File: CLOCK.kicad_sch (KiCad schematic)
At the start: 6 parts, among them X1 S3D50.000000B20F30T

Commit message: DO the bulk of rev 1.2 layout
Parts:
- removed JP3: CLK_EN pull, Jumper:SolderJumper-3_P1.3mm_Bridged12_RoundedPad1.0x1.5mm, symbol Jumper:SolderJumper_3_Bridged12
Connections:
- net CLK_EN: now also R24.1; no longer R24.2
- net GND: now also R24.2
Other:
- moved on the sheet: R24
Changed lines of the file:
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@@
 	(paper "A4")
+	(junction
+		(at 127 96.52)
+		(diameter 0)
+		(color 0 0 0 0)
+	)
 	(junction
 		(at 134.62 96.52)
@@
 	(wire
 		(pts
-			(xy 134.62 80.01) (xy 134.62 85.09)
-		)
-		(stroke
-			(width 0)
-			(type default)
-		)
-	)
-	(wire
-		(pts
 			(xy 153.035 83.82) (xy 153.035 88.9)
 		)
@@
 	(wire
 		(pts
-			(xy 127 76.2) (xy 127 80.01)
-		)
-		(stroke
-			(width 0)
-			(type default)
-		)
-	)
-	(wire
-		(pts
 			(xy 188.595 100.33) (xy 188.595 103.505)
 		)
@@
 	(wire
 		(pts
-			(xy 142.24 76.2) (xy 142.24 72.39)
-		)
-		(stroke
-			(width 0)
-			(type default)
-		)
-	)
-	(wire
-		(pts
-			(xy 134.62 96.52) (xy 134.62 92.71)
-		)
-		(stroke
-			(width 0)
-			(type default)
-		)
-	)
-	(wire
-		(pts
-			(xy 127.635 96.52) (xy 134.62 96.52)
+			(xy 127 107.95) (xy 127 111.76)
+		)
+		(stroke
+			(width 0)
+			(type default)
+		)
+	)
+	(wire
+		(pts
+			(xy 127 96.52) (xy 134.62 96.52)
+		)
+		(stroke
+			(width 0)
+			(type default)
+		)
+	)
+	(wire
+		(pts
+			(xy 118.11 96.52) (xy 127 96.52)
 		)
 		(stroke
@@
 	(wire
 		(pts
-			(xy 139.7 76.2) (xy 142.24 76.2)
-		)
-		(stroke
-			(width 0)
-			(type default)
-		)
-	)
-	(wire
-		(pts
-			(xy 127 76.2) (xy 129.54 76.2)
+			(xy 127 96.52) (xy 127 100.33)
 		)
 		(stroke
@@
 	(hierarchical_label "CLK_EN"
 		(shape input)
-		(at 127.635 96.52 180)
+		(at 118.11 96.52 180)
 		(effects
 			(font
@@
 	(symbol
 		(lib_id "power:GND")
-		(at 127 80.01 0)
+		(at 127 111.76 0)
 		(unit 1)
 		(exclude_from_sim no)
@@
 		(fields_autoplaced yes)
 		(property "Reference" "#PWR08"
-			(at 127 86.36 0)
+			(at 127 118.11 0)
 			(effects
 				(font
@@
 		)
 		(property "Value" "GND"
-			(at 127 85.09 0)
+			(at 127 116.84 0)
 			(effects
 				(font
@@
 		)
 		(property "Footprint" ""
-			(at 127 80.01 0)
+			(at 127 111.76 0)
 			(effects
 				(font
@@
 		)
 		(property "Datasheet" ""
-			(at 127 80.01 0)
+			(at 127 111.76 0)
 			(effects
 				(font
@@
 		)
 		(property "Description" ""
-			(at 127 80.01 0)
+			(at 127 111.76 0)
 			(effects
 				(font
@@
 	(symbol
 		(lib_id "Device:R")
-		(at 134.62 88.9 0)
+		(at 127 104.14 0)
 		(unit 1)
 		(exclude_from_sim no)
@@
 		(on_board yes)
 		(dnp no)
-		(fields_autoplaced yes)
 		(property "Reference" "R24"
-			(at 137.16 87.6299 0)
+			(at 120.396 102.616 0)
 			(effects
 				(font
@@
 		)
 		(property "Value" "10k"
-			(at 137.16 90.1699 0)
+			(at 120.396 105.156 0)
 			(effects
 				(font
@@
 		)
 		(property "Footprint" "Resistor_SMD:R_0603_1608Metric_Pad0.98x0.95mm_HandSolder"
-			(at 132.842 88.9 90)
+			(at 125.222 104.14 90)
 			(effects
 				(font
@@
 		)
 		(property "Datasheet" "~"
-			(at 134.62 88.9 0)
+			(at 127 104.14 0)
 			(effects
 				(font
@@
 		)
 		(property "Description" ""
-			(at 134.62 88.9 0)
+			(at 127 104.14 0)
 			(effects
 				(font
@@
 		)
 		(property "LCSC" "C2930027"
-			(at 134.62 88.9 0)
+			(at 127 104.14 0)
 			(effects
 				(font
@@
 					(unit 1)
 				)
-			)
-		)
-	)
-	(symbol
-		(lib_id "power:+3.3V")
-		(at 142.24 72.39 0)
-		(unit 1)
-		(exclude_from_sim no)
-		(in_bom yes)
-		(on_board yes)
-		(dnp no)
-		(fields_autoplaced yes)
-		(property "Reference" "#PWR049"
-			(at 142.24 76.2 0)
-			(effects
-				(font
-					(size 1.27 1.27)
-				)
-				(hide yes)
-			)
-		)
-		(property "Value" "+3.3V"
-			(at 142.24 67.31 0)
-			(effects
-				(font
-					(size 1.27 1.27)
-				)
-			)
-		)
-		(property "Footprint" ""
-			(at 142.24 72.39 0)
-			(effects
-				(font
-					(size 1.27 1.27)
-				)
-				(hide yes)
-			)
-		)
-		(property "Datasheet" ""
-			(at 142.24 72.39 0)
-			(effects
-				(font
-					(size 1.27 1.27)
-				)
-				(hide yes)
-			)
-		)
-		(property "Description" ""
-			(at 142.24 72.39 0)
-			(effects
-				(font
-					(size 1.27 1.27)
-				)
-				(hide yes)
-			)
-		)
-		(pin "1"
-		)
-		(instances
-			(project ""
-				(path "/727d6c0a-a0ef-4feb-9656-3db3cb90564a/2418ed7a-6668-472e-9550-09c70e5c9c72"
-					(reference "#PWR049")
-					(unit 1)
-				)
-			)
-		)
-	)
-	(symbol
-		(lib_id "Jumper:SolderJumper_3_Bridged12")
-		(at 134.62 76.2 0)
-		(unit 1)
-		(exclude_from_sim yes)
-		(in_bom no)
-		(on_board yes)
-		(dnp no)
-		(fields_autoplaced yes)
-		(property "Reference" "JP3"
-			(at 134.62 69.85 0)
-			(effects
-				(font
-					(size 1.27 1.27)
-				)
-			)
-		)
-		(property "Value" "CLK_EN pull"
-			(at 134.62 72.39 0)
-			(effects
-				(font
-					(size 1.27 1.27)
-				)
-			)
-		)
-		(property "Footprint" "Jumper:SolderJumper-3_P1.3mm_Bridged12_RoundedPad1.0x1.5mm"
-			(at 134.62 76.2 0)
-			(effects
-				(font
-					(size 1.27 1.27)
-				)
-				(hide yes)
-			)
-		)
-		(property "Datasheet" "~"
-			(at 134.62 76.2 0)
-			(effects
-				(font
-					(size 1.27 1.27)
-				)
-				(hide yes)
-			)
-		)
-		(property "Description" "3-pole Solder Jumper, pins 1+2 closed/bridged"
-			(at 134.62 76.2 0)
-			(effects
-				(font
-					(size 1.27 1.27)
-				)
-				(hide yes)
-			)
-		)
-		(pin "1"
-		)
-		(pin "2"
-		)
-		(pin "3"
-		)
-		(instances
-			(project ""
-				(path "/727d6c0a-a0ef-4feb-9656-3db3cb90564a/2418ed7a-6668-472e-9550-09c70e5c9c72"
-					(reference "JP3")
-					(unit 1)
-				)

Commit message: Use kicad symbol for the optotransistor
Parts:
- X1: footprint project specific:XTAL_TSX-3225_16.0000MF18X-AC3 -> project_footprints:XTAL_TSX-3225_16.0000MF18X-AC3
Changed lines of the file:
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@@
 			)
 		)
-		(property "Footprint" "project specific:XTAL_TSX-3225_16.0000MF18X-AC3"
+		(property "Footprint" "project_footprints:XTAL_TSX-3225_16.0000MF18X-AC3"
 			(at 170.815 105.41 0)
 			(effects

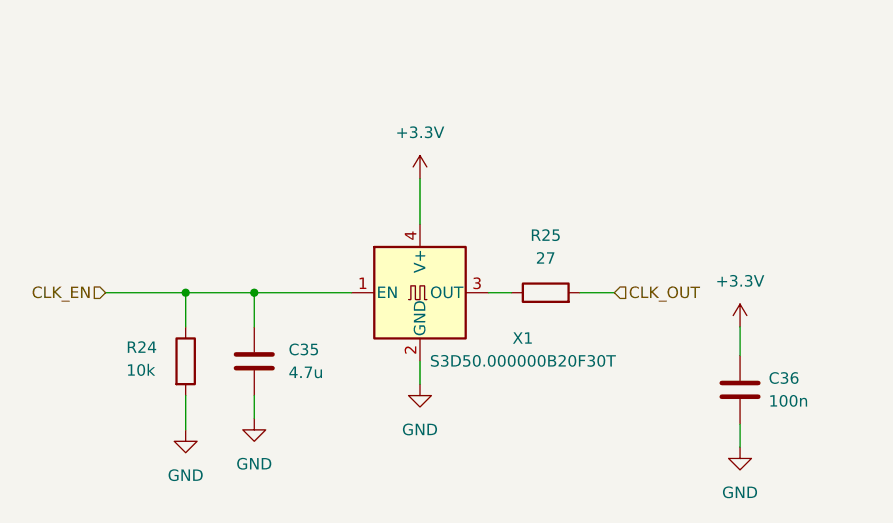
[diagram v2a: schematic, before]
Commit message: Update crystal LCSC number, use built-in footprint
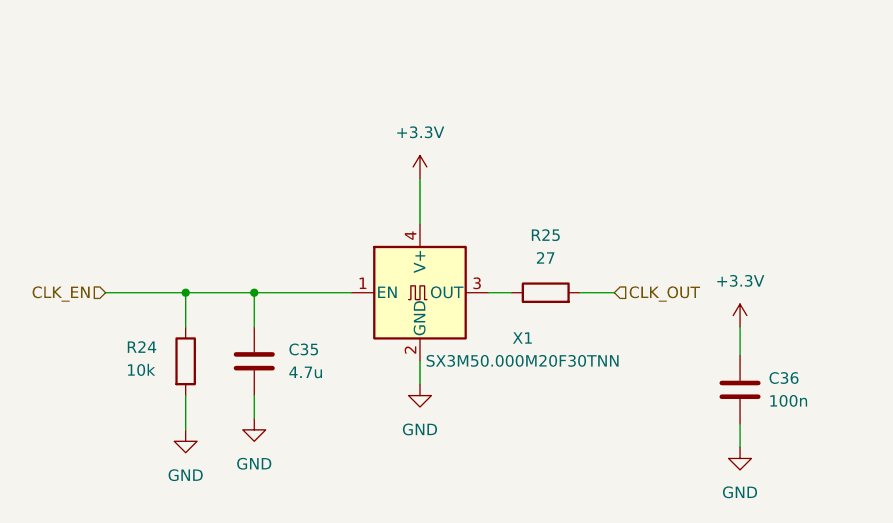
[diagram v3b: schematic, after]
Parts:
- X1: value S3D50.000000B20F30T -> SX3M50.000M20F30TNN; footprint project_footprints:XTAL_TSX-3225_16.0000MF18X-AC3 -> Oscillator:Oscillator_SMD_EuroQuartz_XO32-4Pin_3.2x2.5mm; LCSC C387445 -> C2901592
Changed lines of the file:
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@@
 			)
 		)
-		(property "Value" "S3D50.000000B20F30T"
+		(property "Value" "SX3M50.000M20F30TNN"
 			(at 164.465 104.14 0)
 			(effects
@@
 			)
 		)
-		(property "Footprint" "project_footprints:XTAL_TSX-3225_16.0000MF18X-AC3"
+		(property "Footprint" "Oscillator:Oscillator_SMD_EuroQuartz_XO32-4Pin_3.2x2.5mm"
 			(at 170.815 105.41 0)
 			(effects
@@
 			)
 		)
-		(property "Datasheet" "https://www.lcsc.com/datasheet/lcsc_datasheet_2209071730_Shenzhen-SCTF-Elec-S3D50-000000B20F30T_C387445.pdf"
+		(property "Datasheet" "https://www.lcsc.com/datasheet/C2901592.pdf"
 			(at 150.495 96.52 0)
 			(effects
@@
 			)
 		)
-		(property "LCSC" "C387445"
+		(property "LCSC" "C2901592"
 			(at 153.035 96.52 0)
 			(effects

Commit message: Zamkonator rev 1.3
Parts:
- renumbered C35 to C37, C36 to C38, R24 to R32, R25 to R33
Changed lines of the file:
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@@
 		(dnp no)
 		(fields_autoplaced yes)
-		(property "Reference" "#PWR053"
+		(property "Reference" "#PWR092"
 			(at 188.595 104.14 0)
 			(hide yes)
@@
 			(project "Zamkonator"
 				(path "/727d6c0a-a0ef-4feb-9656-3db3cb90564a/2418ed7a-6668-472e-9550-09c70e5c9c72"
-					(reference "#PWR053")
+					(reference "#PWR092")
 					(unit 1)
 				)
@@
 		(dnp no)
 		(fields_autoplaced yes)
-		(property "Reference" "C36"
+		(property "Reference" "C38"
 			(at 191.77 106.0449 0)
 			(show_name no)
@@
 			(project "Zamkonator"
 				(path "/727d6c0a-a0ef-4feb-9656-3db3cb90564a/2418ed7a-6668-472e-9550-09c70e5c9c72"
-					(reference "C36")
+					(reference "C38")
 					(unit 1)
 				)
@@
 		(dnp no)
 		(fields_autoplaced yes)
-		(property "Reference" "#PWR054"
+		(property "Reference" "#PWR093"
 			(at 188.595 120.015 0)
 			(hide yes)
@@
 			(project "Zamkonator"
 				(path "/727d6c0a-a0ef-4feb-9656-3db3cb90564a/2418ed7a-6668-472e-9550-09c70e5c9c72"
-					(reference "#PWR054")
+					(reference "#PWR093")
 					(unit 1)
 				)
@@
 		(dnp no)
 		(fields_autoplaced yes)
-		(property "Reference" "#PWR08"
+		(property "Reference" "#PWR088"
 			(at 127 118.11 0)
 			(hide yes)
@@
 			(project "Zamkonator"
 				(path "/727d6c0a-a0ef-4feb-9656-3db3cb90564a/2418ed7a-6668-472e-9550-09c70e5c9c72"
-					(reference "#PWR08")
+					(reference "#PWR088")
 					(unit 1)
 				)
@@
 		(dnp no)
 		(fields_autoplaced yes)
-		(property "Reference" "#PWR050"
+		(property "Reference" "#PWR089"
 			(at 134.62 116.84 0)
 			(hide yes)
@@
 			(project "Zamkonator"
 				(path "/727d6c0a-a0ef-4feb-9656-3db3cb90564a/2418ed7a-6668-472e-9550-09c70e5c9c72"
-					(reference "#PWR050")
+					(reference "#PWR089")
 					(unit 1)
 				)
@@
 		(in_pos_files yes)
 		(dnp no)
-		(property "Reference" "R24"
+		(property "Reference" "R32"
 			(at 120.396 102.616 0)
 			(show_name no)
@@
 			(project "Zamkonator"
 				(path "/727d6c0a-a0ef-4feb-9656-3db3cb90564a/2418ed7a-6668-472e-9550-09c70e5c9c72"
-					(reference "R24")
+					(reference "R32")
 					(unit 1)
 				)
@@
 		(dnp no)
 		(fields_autoplaced yes)
-		(property "Reference" "R25"
+		(property "Reference" "R33"
 			(at 167.005 90.17 90)
 			(show_name no)
@@
 			(project "Zamkonator"
 				(path "/727d6c0a-a0ef-4feb-9656-3db3cb90564a/2418ed7a-6668-472e-9550-09c70e5c9c72"
-					(reference "R25")
+					(reference "R33")
 					(unit 1)
 				)
@@
 		(dnp no)
 		(fields_autoplaced yes)
-		(property "Reference" "#PWR052"
+		(property "Reference" "#PWR091"
 			(at 153.035 113.03 0)
 			(hide yes)
@@
 			(project "Zamkonator"
 				(path "/727d6c0a-a0ef-4feb-9656-3db3cb90564a/2418ed7a-6668-472e-9550-09c70e5c9c72"
-					(reference "#PWR052")
+					(reference "#PWR091")
 					(unit 1)
 				)
@@
 		(dnp no)
 		(fields_autoplaced yes)
-		(property "Reference" "#PWR051"
+		(property "Reference" "#PWR090"
 			(at 153.035 87.63 0)
 			(hide yes)
@@
 			(project "Zamkonator"
 				(path "/727d6c0a-a0ef-4feb-9656-3db3cb90564a/2418ed7a-6668-472e-9550-09c70e5c9c72"
-					(reference "#PWR051")
+					(reference "#PWR090")
 					(unit 1)
 				)
@@
 		(dnp no)
 		(fields_autoplaced yes)
-		(property "Reference" "C35"
+		(property "Reference" "C37"
 			(at 138.43 102.8699 0)
 			(show_name no)
@@
 			(project "Zamkonator"
 				(path "/727d6c0a-a0ef-4feb-9656-3db3cb90564a/2418ed7a-6668-472e-9550-09c70e5c9c72"
-					(reference "C35")
+					(reference "C37")
 					(unit 1)
 				)

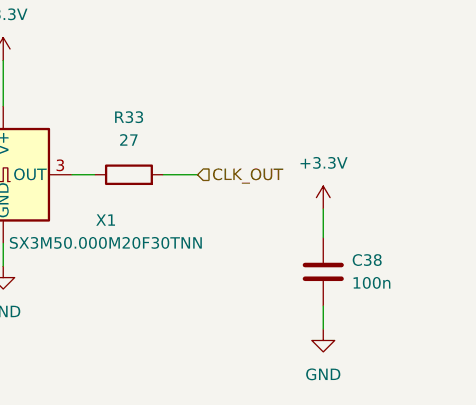
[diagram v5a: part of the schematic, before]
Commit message: Rev 1.3, BOM optimizations
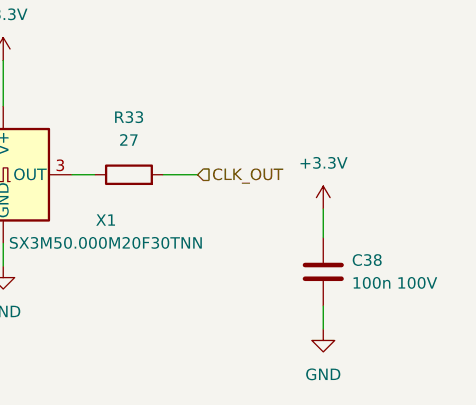
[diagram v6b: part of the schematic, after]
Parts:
- C38: value 100n -> 100n 100V
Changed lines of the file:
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@@
 			)
 		)
-		(property "Value" "100n"
+		(property "Value" "100n 100V"
 			(at 191.77 108.5849 0)
 			(show_name no)
